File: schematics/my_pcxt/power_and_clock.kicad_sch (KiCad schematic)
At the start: 36 parts, among them CON1 BARREL_JACK, P1 Conn_01x02_Male, SW1 RESET_8088, U2 7805, U3 8284, Y1 6-30 MHz

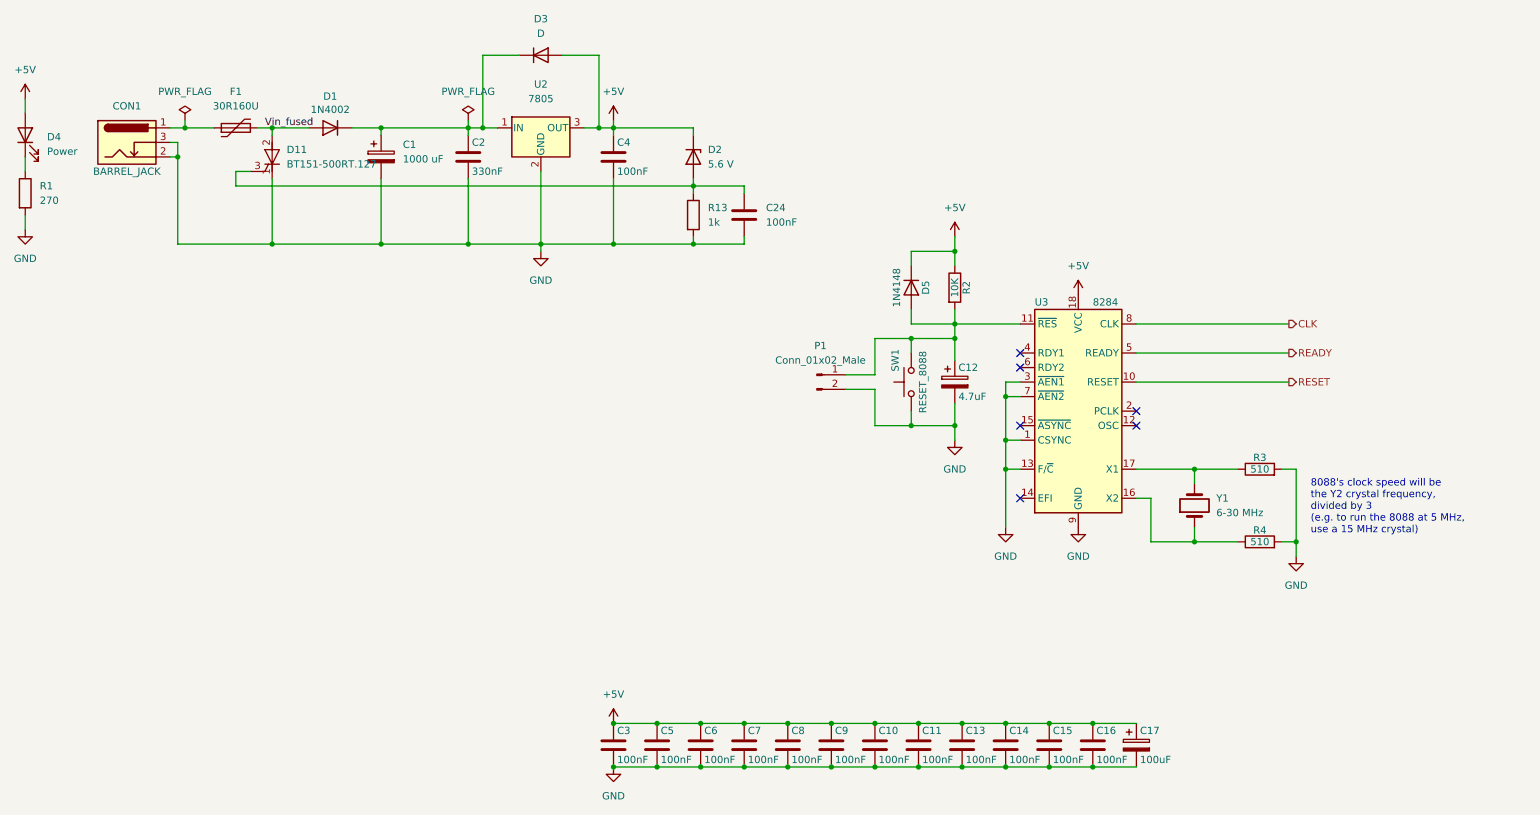
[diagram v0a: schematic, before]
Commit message: Implemented 8259 e 8253
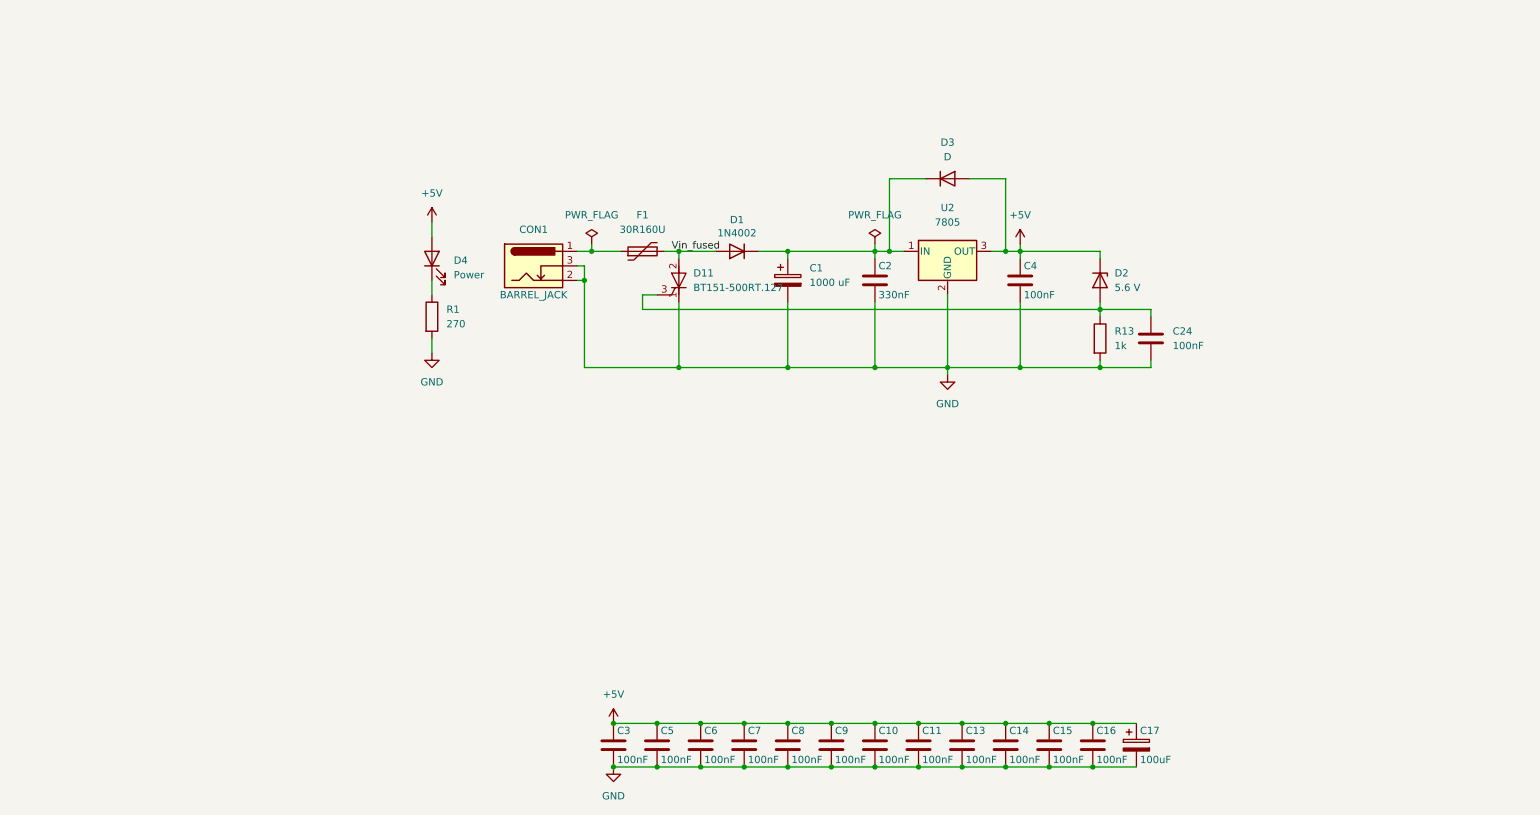
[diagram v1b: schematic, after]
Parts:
- removed C12: 4.7uF, Capacitor_THT:CP_Radial_D5.0mm_P2.00mm, symbol Device:C_Polarized
- removed D5: 1N4148, Diode_THT:D_DO-35_SOD27_P7.62mm_Horizontal, symbol Device:D
- removed P1: Conn_01x02_Male, Connector_PinHeader_2.54mm:PinHeader_1x02_P2.54mm_Vertical, symbol Connector:Conn_01x02_Male
- removed R2: 10K, Resistor_THT:R_Axial_DIN0207_L6.3mm_D2.5mm_P10.16mm_Horizontal, symbol Device:R
- removed R3, R4: 510, Resistor_THT:R_Axial_DIN0207_L6.3mm_D2.5mm_P10.16mm_Horizontal, symbol Device:R
- removed SW1: RESET_8088, Button_Switch_THT:SW_PUSH_6mm_H5mm, symbol Switch:SW_Push
- removed U3: 8284, Package_DIP:DIP-18_W7.62mm, symbol Timer:8284
- removed Y1: 6-30 MHz, Crystal:Crystal_HC49-U_Vertical, symbol Device:Crystal
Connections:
- no-connect marks 6 -> 0
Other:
- note removed: "8088's clock speed will be the Y2 crystal frequency, divided by 3 (e.g. to run the 8088 at 5 MHz, use a 15 MHz crystal)"
- moved on the sheet: C1, C2, C24, C4, CON1, D1, D11, D2, D3, D4, F1, R1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
